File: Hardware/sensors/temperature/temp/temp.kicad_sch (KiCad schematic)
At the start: 3 parts, among them J1 Conn_01x03_Socket, J2 Conn_01x03_Socket, U1 TMP1826DGK

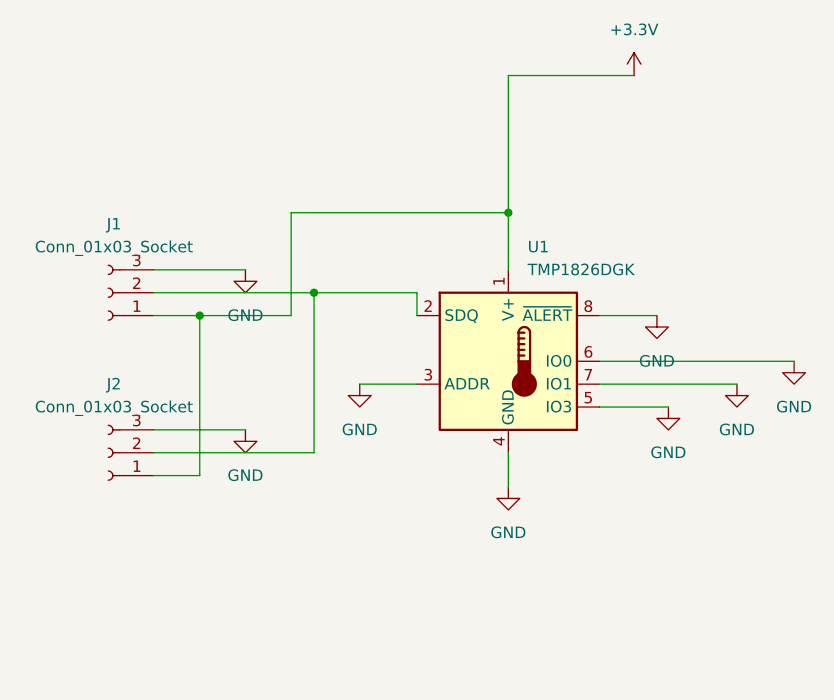
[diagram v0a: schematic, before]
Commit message: improved temperature 1-wire pcb
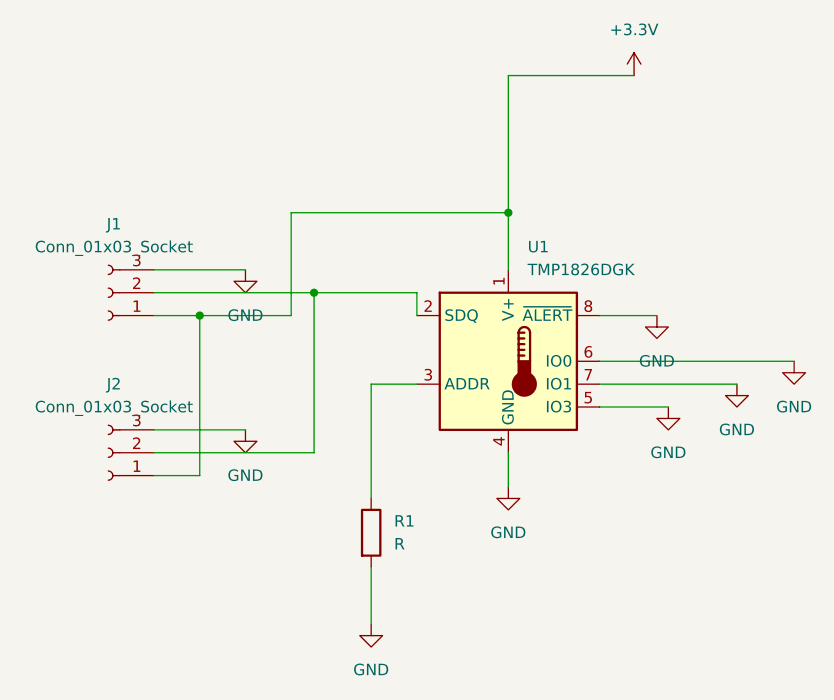
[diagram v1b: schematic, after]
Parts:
- added R1: R, Resistor_SMD:R_0805_2012Metric_Pad1.20x1.40mm_HandSolder, symbol Device:R
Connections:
- net GND: now also R1.2; no longer U1.3 (ADDR)
- new net: R1.1, U1.3 (ADDR)
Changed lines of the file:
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@@
+	(wire
+		(pts
+			(xy 100.33 114.3) (xy 100.33 101.6)
+		)
+		(stroke
+			(width 0)
+			(type default)
+		)
+	)
+	(wire
+		(pts
+			(xy 100.33 128.27) (xy 100.33 121.92)
+		)
+		(stroke
+			(width 0)
+			(type default)
+		)
+	)
 	(wire
 		(pts
@@
 	(wire
 		(pts
+			(xy 100.33 101.6) (xy 105.41 101.6)
+		)
+		(stroke
+			(width 0)
+			(type default)
+		)
+	)
+	(wire
+		(pts
 			(xy 115.57 88.9) (xy 115.57 82.55)
 		)
@@
 		(pts
 			(xy 76.2 109.22) (xy 93.98 109.22)
-		)
-		(stroke
-			(width 0)
-			(type default)
-		)
-	)
-	(wire
-		(pts
-			(xy 99.06 101.6) (xy 105.41 101.6)
 		)
 		(stroke
@@
 	)
 	(symbol
+		(lib_id "Device:R")
+		(at 100.33 118.11 0)
+		(unit 1)
+		(exclude_from_sim no)
+		(in_bom yes)
+		(on_board yes)
+		(dnp no)
+		(fields_autoplaced yes)
+		(property "Reference" "R1"
+			(at 102.87 116.8399 0)
+			(effects
+				(font
+					(size 1.27 1.27)
+				)
+				(justify left)
+			)
+		)
+		(property "Value" "R"
+			(at 102.87 119.3799 0)
+			(effects
+				(font
+					(size 1.27 1.27)
+				)
+				(justify left)
+			)
+		)
+		(property "Footprint" "Resistor_SMD:R_0805_2012Metric_Pad1.20x1.40mm_HandSolder"
+			(at 98.552 118.11 90)
+			(effects
+				(font
+					(size 1.27 1.27)
+				)
+				(hide yes)
+			)
+		)
+		(property "Datasheet" "~"
+			(at 100.33 118.11 0)
+			(effects
+				(font
+					(size 1.27 1.27)
+				)
+				(hide yes)
+			)
+		)
+		(property "Description" "Resistor"
+			(at 100.33 118.11 0)
+			(effects
+				(font
+					(size 1.27 1.27)
+				)
+				(hide yes)
+			)
+		)
+		(pin "2"
+		)
+		(pin "1"
+		)
+		(instances
+			(project "temp"
+				(path "/b5a1c361-04ae-4923-b6c2-708ee26a336b"
+					(reference "R1")
+					(unit 1)
+				)
+			)
+		)
+	)
+	(symbol
 		(lib_id "Connector:Conn_01x03_Socket")
 		(at 71.12 109.22 180)
@@
 	(symbol
 		(lib_id "power:GND")
-		(at 99.06 101.6 0)
+		(at 100.33 128.27 0)
 		(unit 1)
 		(exclude_from_sim no)
@@
 		(fields_autoplaced yes)
 		(property "Reference" "#PWR06"
-			(at 99.06 107.95 0)
+			(at 100.33 134.62 0)
 			(effects
 				(font
@@
 		)
 		(property "Value" "GND"
-			(at 99.06 106.68 0)
+			(at 100.33 133.35 0)
 			(effects
 				(font
@@
 		)
 		(property "Footprint" ""
-			(at 99.06 101.6 0)
+			(at 100.33 128.27 0)
 			(effects
 				(font
@@
 		)
 		(property "Datasheet" ""
-			(at 99.06 101.6 0)
+			(at 100.33 128.27 0)
 			(effects
 				(font
@@
 		)
 		(property "Description" "Power symbol creates a global label with name \"GND\" , ground"
-			(at 99.06 101.6 0)
-			(effects
-				(font
+			(at 100.33 128.27 0)
+			(effects
+				(font
